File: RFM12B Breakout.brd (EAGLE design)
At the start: 22.9 x 36.2 mm, 6 parts, among them U1 RFM12B

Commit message: Edited silkscreen text to ensure minimum 5mil width for OSHPark.
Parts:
- moved U$1 0.63 mm to (17.8, 27.9)
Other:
- board text added: "RFM12B Breakout 1.0"
- board text removed: "RFM12B Breakout"
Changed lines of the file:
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@@
 <setting verticaltext="up"/>
 </settings>
-<grid distance="0.025" unitdist="inch" unit="inch" style="lines" multiple="1" display="yes" altdistance="0.025" altunitdist="inch" altunit="inch"/>
+<grid distance="0.005" unitdist="inch" unit="inch" style="lines" multiple="1" display="yes" altdistance="0.025" altunitdist="inch" altunit="inch"/>
 <layers>
 <layer number="1" name="Top" color="4" fill="1" visible="yes" active="yes"/>
@@
 <wire x1="16.51" y1="18.415" x2="22.86" y2="18.415" width="0" layer="20"/>
 <wire x1="22.86" y1="36.195" x2="22.86" y2="18.415" width="0" layer="20"/>
-<text x="8.255" y="17.145" size="0.8128" layer="21" font="fixed">GND</text>
-<text x="12.065" y="12.065" size="0.8128" layer="21" font="fixed" rot="R180">GND</text>
-<text x="8.255" y="14.605" size="0.8128" layer="21" font="fixed">NRES</text>
-<text x="8.255" y="12.065" size="0.8128" layer="21" font="fixed">CLK</text>
-<text x="8.255" y="9.525" size="0.8128" layer="21" font="fixed">DCLK</text>
-<text x="8.255" y="6.985" size="0.8128" layer="21" font="fixed">FSK</text>
-<text x="8.255" y="4.445" size="0.8128" layer="21" font="fixed">NIRQ</text>
-<text x="8.255" y="1.905" size="0.8128" layer="21" font="fixed">SDO</text>
-<text x="12.065" y="9.525" size="0.8128" layer="21" font="fixed" rot="R180">NINT</text>
-<text x="12.065" y="6.985" size="0.8128" layer="21" font="fixed" rot="R180">SDI</text>
-<text x="12.065" y="4.445" size="0.8128" layer="21" font="fixed" rot="R180">SCK</text>
-<text x="12.065" y="1.905" size="0.8128" layer="21" font="fixed" rot="R180">NSEL</text>
-<text x="12.065" y="14.605" size="0.8128" layer="21" font="fixed" rot="R180">VDD</text>
-<text x="12.065" y="17.145" size="0.8128" layer="21" font="fixed" rot="R180">ANT</text>
-<text x="21.59" y="33.02" size="1.4224" layer="22" font="fixed" rot="MR0">RFM12B Breakout</text>
-<text x="21.59" y="31.115" size="1.27" layer="22" font="fixed" rot="MR0">Alex Whittemore</text>
-<text x="15.24" y="29.21" size="1.27" layer="22" font="fixed" rot="MR0">CC BY-SA 3.0</text>
-<text x="21.59" y="26.035" size="0.8128" layer="22" font="fixed" rot="MR0">Some parts CC-BY-SA</text>
-<text x="21.59" y="24.765" size="0.8128" layer="22" font="fixed" rot="MR0">Sparkfun Electronics</text>
+<text x="8.255" y="17.145" size="0.8128" layer="21" font="vector" ratio="15">GND</text>
+<text x="12.065" y="12.065" size="0.8128" layer="21" font="vector" ratio="15" rot="R180">GND</text>
+<text x="8.255" y="14.605" size="0.8128" layer="21" font="vector" ratio="15">NRES</text>
+<text x="8.255" y="12.065" size="0.8128" layer="21" font="vector" ratio="15">CLK</text>
+<text x="8.255" y="9.525" size="0.8128" layer="21" font="vector" ratio="15">DCLK</text>
+<text x="8.255" y="6.985" size="0.8128" layer="21" font="vector" ratio="15">FSK</text>
+<text x="8.255" y="4.445" size="0.8128" layer="21" font="vector" ratio="15">NIRQ</text>
+<text x="8.255" y="1.905" size="0.8128" layer="21" font="vector" ratio="15">SDO</text>
+<text x="12.065" y="9.525" size="0.8128" layer="21" font="vector" ratio="15" rot="R180">NINT</text>
+<text x="12.065" y="6.985" size="0.8128" layer="21" font="vector" ratio="15" rot="R180">SDI</text>
+<text x="12.065" y="4.445" size="0.8128" layer="21" font="vector" ratio="15" rot="R180">SCK</text>
+<text x="12.065" y="1.905" size="0.8128" layer="21" font="vector" ratio="15" rot="R180">NSEL</text>
+<text x="12.065" y="14.605" size="0.8128" layer="21" font="vector" ratio="15" rot="R180">VDD</text>
+<text x="12.065" y="17.145" size="0.8128" layer="21" font="vector" ratio="15" rot="R180">ANT</text>
+<text x="21.59" y="33.02" size="1.27" layer="22" font="vector" ratio="10" rot="MR0">RFM12B Breakout 1.0</text>
+<text x="21.59" y="31.75" size="1.016" layer="22" font="vector" ratio="12" rot="MR0">Alex Whittemore</text>
+<text x="14.605" y="27.94" size="1.27" layer="22" font="vector" ratio="10" rot="MR0">CC BY-SA 3.0</text>
+<text x="22.225" y="20.32" size="0.8128" layer="22" font="vector" ratio="15" rot="MR0">Some parts CC-BY-SA</text>
+<text x="22.225" y="19.05" size="0.8128" layer="22" font="vector" ratio="15" rot="MR0">Sparkfun Electronics</text>
 </plain>
 <attributes>
@@
 </element>
 <element name="ANT" library="SparkFun-Connectors" package="1X01" value="" x="20.95" y="23.6" smashed="yes">
-<attribute name="NAME" x="21.5612" y="25.3188" size="1.27" layer="25" font="fixed" rot="R90"/>
+<attribute name="NAME" x="21.5612" y="25.3188" size="1.27" layer="25" font="vector" ratio="10" rot="R90"/>
 <attribute name="VALUE" x="22.855" y="23.6" size="1.27" layer="27"/>
 </element>
 <element name="SJ1" library="BUBB-Eagle-Library" package="SJ_2S-NO" value="" x="20.955" y="20.955" rot="R270"/>
 <element name="U1" library="AlexW-Eagle-Libraries" package="RFM12-XXX-S2" value="RFM12B" x="10.16" y="27.305"/>
-<element name="U$1" library="SparkFun-Aesthetics" package="OSHW-LOGO-M" value="" x="17.78" y="28.575" rot="MR0"/>
+<element name="U$1" library="SparkFun-Aesthetics" package="OSHW-LOGO-M" value="" x="17.78" y="27.94" rot="MR0"/>
 </elements>
 <signals>

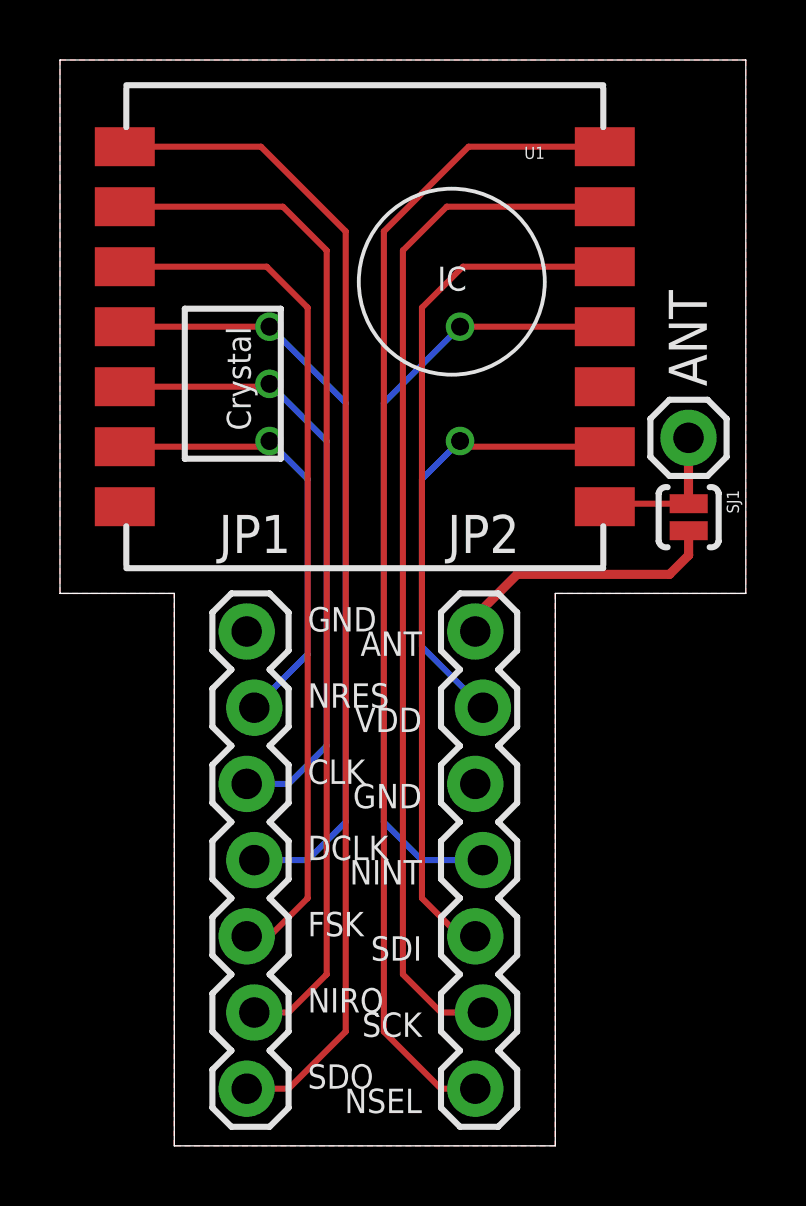
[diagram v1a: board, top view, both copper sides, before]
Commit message: Beefed up the power trace to 16mil as it should have been all along. Probably not a problem in R1, but definitely something to touch up.
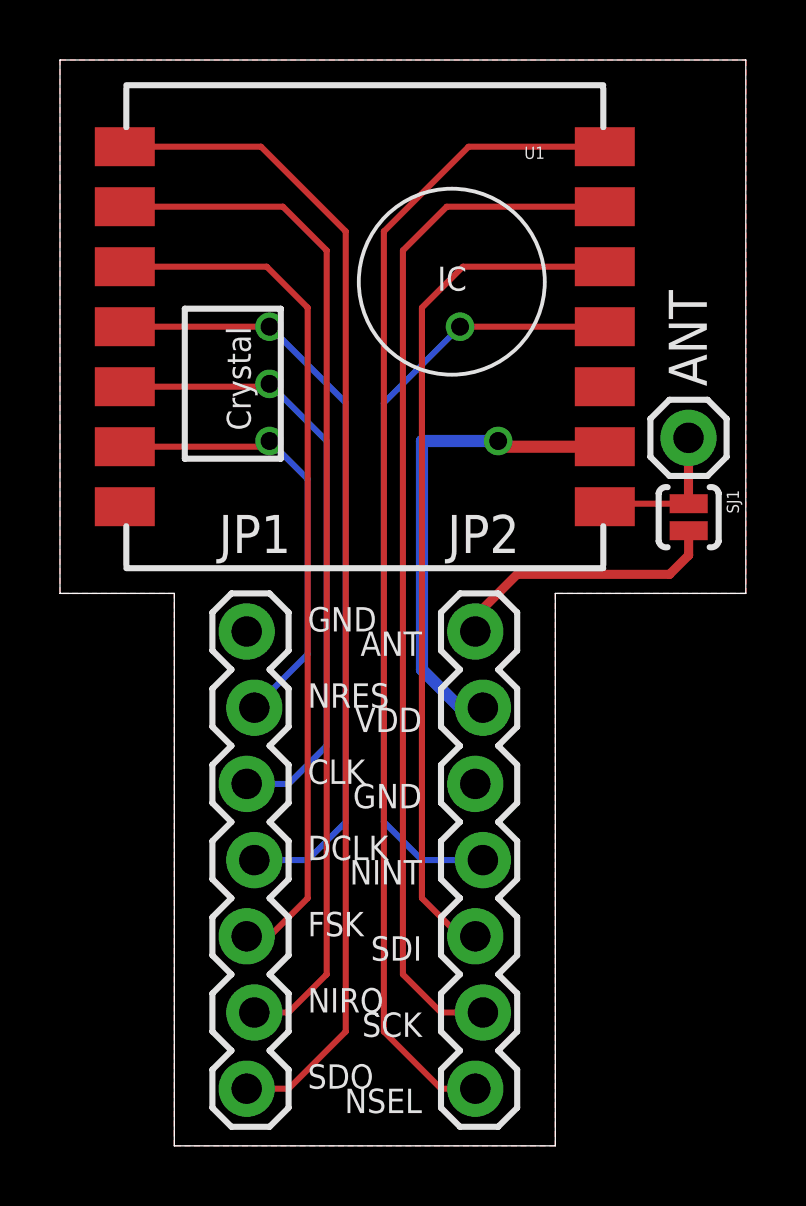
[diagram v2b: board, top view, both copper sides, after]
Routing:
- net VDD: track 15.3 -> 16.5 mm
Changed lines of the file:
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@@
 <setting verticaltext="up"/>
 </settings>
-<grid distance="0.005" unitdist="inch" unit="inch" style="lines" multiple="1" display="yes" altdistance="0.025" altunitdist="inch" altunit="inch"/>
+<grid distance="0.025" unitdist="inch" unit="inch" style="lines" multiple="1" display="yes" altdistance="0.025" altunitdist="inch" altunit="inch"/>
 <layers>
 <layer number="1" name="Top" color="4" fill="1" visible="yes" active="yes"/>
@@
 <signal name="VDD">
 <contactref element="JP2" pad="6"/>
-<wire x1="14.097" y1="14.605" x2="12.065" y2="16.637" width="0.2032" layer="16"/>
-<wire x1="12.065" y1="16.637" x2="12.065" y2="22.225" width="0.2032" layer="16"/>
-<wire x1="12.065" y1="22.225" x2="13.335" y2="23.495" width="0.2032" layer="16"/>
-<via x="13.335" y="23.495" extent="1-16" drill="0.6" shape="square"/>
 <contactref element="U1" pad="9"/>
-<wire x1="18.16" y1="23.305" x2="13.335" y2="23.305" width="0.2032" layer="1"/>
-<wire x1="13.335" y1="23.305" x2="13.335" y2="23.495" width="0.2032" layer="1"/>
+<wire x1="18.16" y1="23.305" x2="14.605" y2="23.305" width="0.4064" layer="1"/>
+<wire x1="14.605" y1="23.305" x2="14.605" y2="23.495" width="0.4064" layer="1"/>
+<via x="14.605" y="23.495" extent="1-16" drill="0.6" shape="square"/>
+<wire x1="14.605" y1="23.495" x2="12.065" y2="23.495" width="0.4064" layer="16"/>
+<wire x1="12.065" y1="23.495" x2="12.065" y2="15.875" width="0.4064" layer="16"/>
+<wire x1="12.065" y1="15.875" x2="13.335" y2="14.605" width="0.4064" layer="16"/>
+<wire x1="13.335" y1="14.605" x2="14.097" y2="14.605" width="0.4064" layer="16"/>
 </signal>
 <signal name="NIRQ">
